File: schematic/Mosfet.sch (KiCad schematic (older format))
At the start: 35 parts, among them J10 Conn_01x03, J8 Screw_Terminal_01x02, J9 Conn_01x03, Q1 PSMN1R7-30YL, Q2 PSMN1R7-30YL, Q3 NCV8402, Q4 NCV8402

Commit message: Fixed C93 footprint
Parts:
- C93: footprint Resistors_SMD:R_0603 -> Capacitors_SMD:C_0603
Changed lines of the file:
@@
 F 0 "C93" H 9225 3150 50  0000 L CNN
 F 1 "100nF" H 9225 2950 50  0000 L CNN
-F 2 "Resistors_SMD:R_0603" H 9238 2900 50  0001 C CNN
+F 2 "Capacitors_SMD:C_0603" H 9238 2900 50  0001 C CNN
 F 3 "" H 9200 3050 50  0001 C CNN
 	1    9200 3050

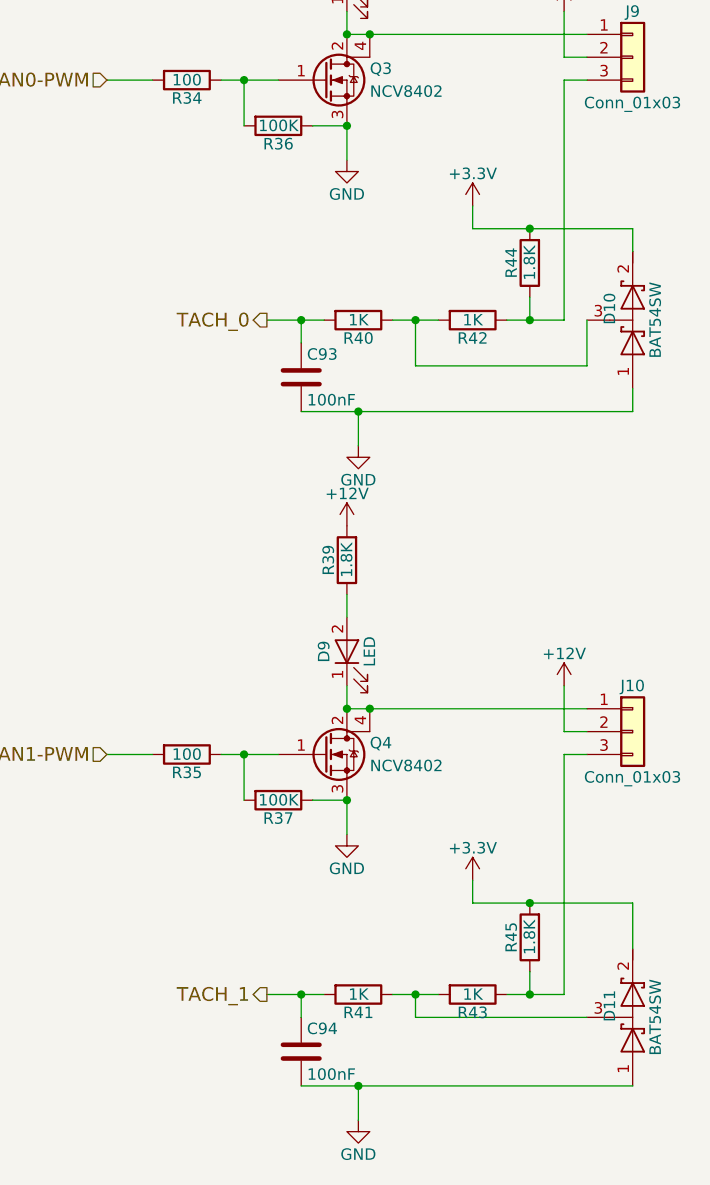
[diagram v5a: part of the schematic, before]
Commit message: Removed some components
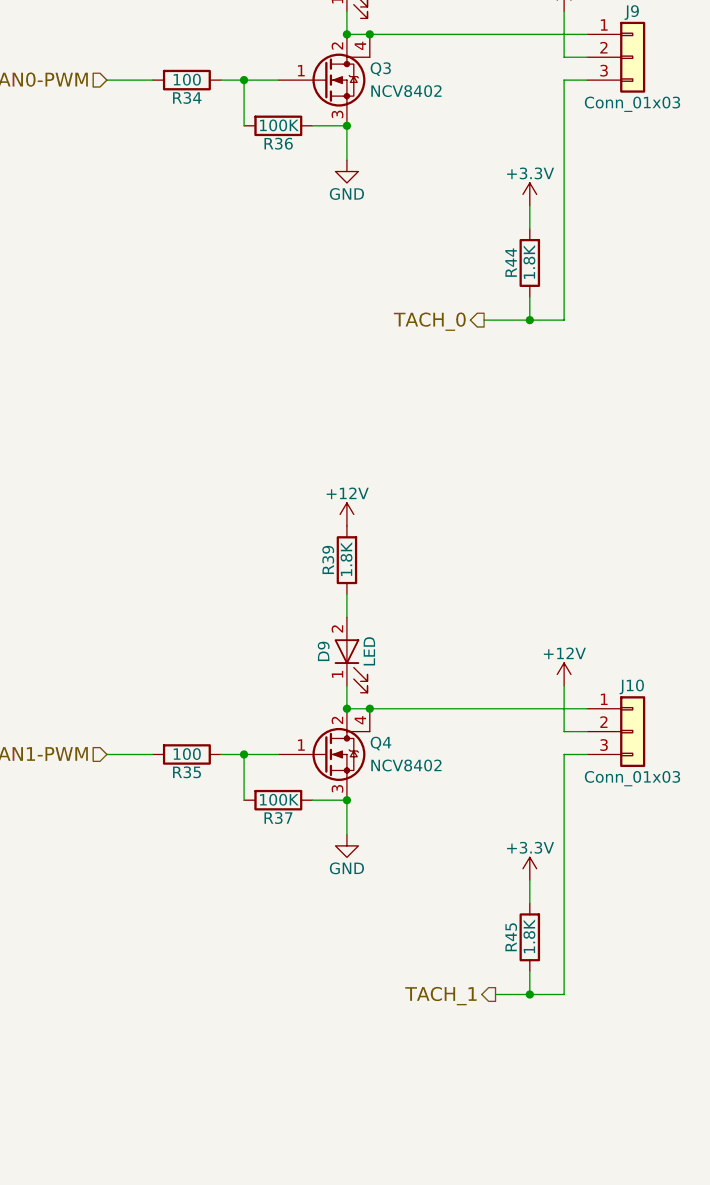
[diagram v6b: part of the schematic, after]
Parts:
- removed C93, C94: 100nF, Capacitors_SMD:C_0603, symbol C
- removed D10, D11: BAT54SW, TO_SOT_Packages_SMD:SOT-323_SC-70, symbol D_Schottky_x2_Serial_AKC
- removed R40, R41, R42, R43: 1K, Resistors_SMD:R_0603, symbol R
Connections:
- net TACH_0: now also J9.3 (Pin_3), R44.1
- net TACH_1: now also J10.3 (Pin_3), R45.1
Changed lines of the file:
@@
 	9400 1950 9400 2100
 $Comp
-L GND #PWR119
+L GND #PWR121
 U 1 1 59EA915F
 P 9400 2100
-F 0 "#PWR119" H 9400 1850 50  0001 C CNN
+F 0 "#PWR121" H 9400 1850 50  0001 C CNN
 F 1 "GND" H 9400 1950 50  0000 C CNN
 F 2 "" H 9400 2100 50  0001 C CNN
@@
 $EndComp
 $Comp
-L +12V #PWR126
+L +12V #PWR120
 U 1 1 59EBB7E0
 P 10350 1450
-F 0 "#PWR126" H 10350 1300 50  0001 C CNN
+F 0 "#PWR120" H 10350 1300 50  0001 C CNN
 F 1 "+12V" H 10350 1590 50  0000 C CNN
 F 2 "" H 10350 1450 50  0001 C CNN
@@
 Wire Wire Line
 	10350 1650 10350 1450
-$Comp
-L R R40
-U 1 1 59EBB878
-P 9450 2800
-F 0 "R40" V 9530 2800 50  0000 C CNN
-F 1 "1K" V 9450 2800 50  0000 C CNN
-F 2 "Resistors_SMD:R_0603" V 9380 2800 50  0001 C CNN
-F 3 "" H 9450 2800 50  0001 C CNN
-	1    9450 2800
-	0    1    1    0
-$EndComp
-$Comp
-L R R42
-U 1 1 59EBB8DD
-P 9950 2800
-F 0 "R42" V 10030 2800 50  0000 C CNN
-F 1 "1K" V 9950 2800 50  0000 C CNN
-F 2 "Resistors_SMD:R_0603" V 9880 2800 50  0001 C CNN
-F 3 "" H 9950 2800 50  0001 C CNN
-	1    9950 2800
-	0    1    1    0
-$EndComp
 $Comp
 L R R44
@@
 	-1   0    0    1
 $EndComp
-$Comp
-L C C93
-U 1 1 59EBB948
-P 9200 3050
-F 0 "C93" H 9225 3150 50  0000 L CNN
-F 1 "100nF" H 9225 2950 50  0000 L CNN
-F 2 "Capacitors_SMD:C_0603" H 9238 2900 50  0001 C CNN
-F 3 "" H 9200 3050 50  0001 C CNN
-	1    9200 3050
-	1    0    0    -1
-$EndComp
 Wire Wire Line
 	10450 1750 10350 1750
@@
 	10350 1750 10350 2800
 Wire Wire Line
-	10350 2800 10100 2800
+	10350 2800 10000 2800
 Wire Wire Line
 	10200 2800 10200 2700
 Connection ~ 10200 2800
-Wire Wire Line
-	9600 2800 9800 2800
-Connection ~ 9700 2800
-Wire Wire Line
-	9200 3200 10650 3200
-Wire Wire Line
-	9200 2900 9200 2800
-Wire Wire Line
-	9050 2800 9300 2800
-$Comp
-L GND #PWR122
-U 1 1 59EBBD19
-P 9450 3350
-F 0 "#PWR122" H 9450 3100 50  0001 C CNN
-F 1 "GND" H 9450 3200 50  0000 C CNN
-F 2 "" H 9450 3350 50  0001 C CNN
-F 3 "" H 9450 3350 50  0001 C CNN
-	1    9450 3350
-	1    0    0    -1
-$EndComp
-Wire Wire Line
-	9450 3350 9450 3200
-Connection ~ 9450 3200
-Connection ~ 9200 2800
-Text HLabel 9050 2800 0    60   Output ~ 0
+Text HLabel 10000 2800 0    60   Output ~ 0
 TACH_0
 $Comp
-L +3.3V #PWR124
+L +3.3V #PWR122
 U 1 1 59EBBF65
-P 9950 2300
-F 0 "#PWR124" H 9950 2150 50  0001 C CNN
-F 1 "+3.3V" H 9950 2440 50  0000 C CNN
-F 2 "" H 9950 2300 50  0001 C CNN
-F 3 "" H 9950 2300 50  0001 C CNN
-	1    9950 2300
-	1    0    0    -1
-$EndComp
-Wire Wire Line
-	9950 2300 9950 2400
+P 10200 2300
+F 0 "#PWR122" H 10200 2150 50  0001 C CNN
+F 1 "+3.3V" H 10200 2440 50  0000 C CNN
+F 2 "" H 10200 2300 50  0001 C CNN
+F 3 "" H 10200 2300 50  0001 C CNN
+	1    10200 2300
+	1    0    0    -1
+$EndComp
+Wire Wire Line
+	10200 2300 10200 2400
 $Comp
 L Q_NMOS_GDSD Q4
@@
 	9400 4900 9400 5050
 $Comp
-L GND #PWR121
+L GND #PWR128
 U 1 1 59EBE910
 P 9400 5050
-F 0 "#PWR121" H 9400 4800 50  0001 C CNN
+F 0 "#PWR128" H 9400 4800 50  0001 C CNN
 F 1 "GND" H 9400 4900 50  0000 C CNN
 F 2 "" H 9400 5050 50  0001 C CNN
@@
 	8350 4700 8550 4700
 $Comp
-L +12V #PWR120
+L +12V #PWR125
 U 1 1 59EBE919
 P 9400 3700
-F 0 "#PWR120" H 9400 3550 50  0001 C CNN
+F 0 "#PWR125" H 9400 3550 50  0001 C CNN
 F 1 "+12V" H 9400 3840 50  0000 C CNN
 F 2 "" H 9400 3700 50  0001 C CNN
@@
 $EndComp
 $Comp
-L +12V #PWR127
+L +12V #PWR126
 U 1 1 59EBE91F
 P 10350 4400
-F 0 "#PWR127" H 10350 4250 50  0001 C CNN
+F 0 "#PWR126" H 10350 4250 50  0001 C CNN
 F 1 "+12V" H 10350 4540 50  0000 C CNN
 F 2 "" H 10350 4400 50  0001 C CNN
@@
 Wire Wire Line
 	10350 4600 10350 4400
-$Comp
-L R R41
-U 1 1 59EBE927
-P 9450 5750
-F 0 "R41" V 9530 5750 50  0000 C CNN
-F 1 "1K" V 9450 5750 50  0000 C CNN
-F 2 "Resistors_SMD:R_0603" V 9380 5750 50  0001 C CNN
-F 3 "" H 9450 5750 50  0001 C CNN
-	1    9450 5750
-	0    1    1    0
-$EndComp
-$Comp
-L R R43
-U 1 1 59EBE92D
-P 9950 5750
-F 0 "R43" V 10030 5750 50  0000 C CNN
-F 1 "1K" V 9950 5750 50  0000 C CNN
-F 2 "Resistors_SMD:R_0603" V 9880 5750 50  0001 C CNN
-F 3 "" H 9950 5750 50  0001 C CNN
-	1    9950 5750
-	0    1    1    0
-$EndComp
 $Comp
 L R R45
@@
 	-1   0    0    1
 $EndComp
-$Comp
-L C C94
-U 1 1 59EBE939
-P 9200 6000
-F 0 "C94" H 9225 6100 50  0000 L CNN
-F 1 "100nF" H 9225 5900 50  0000 L CNN
-F 2 "Capacitors_SMD:C_0603" H 9238 5850 50  0001 C CNN
-F 3 "" H 9200 6000 50  0001 C CNN
-	1    9200 6000
-	1    0    0    -1
-$EndComp
 Wire Wire Line
 	10450 4700 10350 4700
@@
 	10350 4700 10350 5750
 Wire Wire Line
-	10350 5750 10100 5750
+	10350 5750 10050 5750
 Wire Wire Line
 	10200 5750 10200 5650
 Connection ~ 10200 5750
 Wire Wire Line
-	9600 5750 9800 5750
-Connection ~ 9700 5750
-Wire Wire Line
-	9950 5350 10650 5350
-Wire Wire Line
-	9200 6150 10650 6150
-Wire Wire Line
-	9200 5850 9200 5750
-Wire Wire Line
-	9050 5750 9300 5750
-$Comp
-L GND #PWR123
-U 1 1 59EBE957
-P 9450 6300
-F 0 "#PWR123" H 9450 6050 50  0001 C CNN
-F 1 "GND" H 9450 6150 50  0000 C CNN
-F 2 "" H 9450 6300 50  0001 C CNN
-F 3 "" H 9450 6300 50  0001 C CNN
-	1    9450 6300
-	1    0    0    -1
-$EndComp
-Wire Wire Line
-	9450 6300 9450 6150
-Connection ~ 9450 6150
-Connection ~ 9200 5750
-Text HLabel 9050 5750 0    60   Output ~ 0
+	10200 5350 10200 5350
+Text HLabel 10050 5750 0    60   Output ~ 0
 TACH_1
 $Comp
-L +3.3V #PWR125
+L +3.3V #PWR129
 U 1 1 59EBE961
-P 9950 5250
-F 0 "#PWR125" H 9950 5100 50  0001 C CNN
-F 1 "+3.3V" H 9950 5390 50  0000 C CNN
-F 2 "" H 9950 5250 50  0001 C CNN
-F 3 "" H 9950 5250 50  0001 C CNN
-	1    9950 5250
-	1    0    0    -1
-$EndComp
-Wire Wire Line
-	9950 5250 9950 5350
+P 10200 5250
+F 0 "#PWR129" H 10200 5100 50  0001 C CNN
+F 1 "+3.3V" H 10200 5390 50  0000 C CNN
+F 2 "" H 10200 5250 50  0001 C CNN
+F 3 "" H 10200 5250 50  0001 C CNN
+	1    10200 5250
+	1    0    0    -1
+$EndComp
+Wire Wire Line
+	10200 5250 10200 5350
 Text HLabel 1700 2200 0    60   Input ~ 0
 BED
@@
 $EndComp
 $Comp
-L +24V #PWR114
+L +24V #PWR119
 U 1 1 59EC2711
 P 2350 1400
-F 0 "#PWR114" H 2350 1250 50  0001 C CNN
+F 0 "#PWR119" H 2350 1250 50  0001 C CNN
 F 1 "+24V" H 2350 1540 50  0000 C CNN
 F 2 "" H 2350 1400 50  0001 C CNN
@@
 	2350 2950 2350 2900
 $Comp
-L GND #PWR115
+L GND #PWR123
 U 1 1 59EC2B99
 P 2350 2950
-F 0 "#PWR115" H 2350 2700 50  0001 C CNN
+F 0 "#PWR123" H 2350 2700 50  0001 C CNN
 F 1 "GND" H 2350 2800 50  0000 C CNN
 F 2 "" H 2350 2950 50  0001 C CNN
@@
 	2350 4950 2350 4900
 $Comp
-L GND #PWR117
+L GND #PWR127
 U 1 1 59EC3896
 P 2350 4950
-F 0 "#PWR117" H 2350 4700 50  0001 C CNN
+F 0 "#PWR127" H 2350 4700 50  0001 C CNN
 F 1 "GND" H 2350 4800 50  0000 C CNN
 F 2 "" H 2350 4950 50  0001 C CNN
@@
 Connection ~ 1950 4650
 $Comp
-L VBUS #PWR116
+L VBUS #PWR124
 U 1 1 59EC3DE5
 P 2350 3400
-F 0 "#PWR116" H 2350 3250 50  0001 C CNN
+F 0 "#PWR124" H 2350 3250 50  0001 C CNN
 F 1 "VBUS" H 2350 3550 50  0000 C CNN
 F 2 "" H 2350 3400 50  0001 C CNN
@@
 	1700 3600 1700 4200
 $Comp
-L D_Schottky_x2_Serial_AKC D10
-U 1 1 59F5BB09
-P 10650 2800
-F 0 "D10" H 10700 2700 50  0000 C CNN
-F 1 "BAT54SW" H 10650 2900 50  0000 C CNN
-F 2 "TO_SOT_Packages_SMD:SOT-323_SC-70" H 10650 2800 50  0001 C CNN
-F 3 "" H 10650 2800 50  0001 C CNN
-	1    10650 2800
-	0    1    -1   0
-$EndComp
-Wire Wire Line
-	10650 3200 10650 3100
-Wire Wire Line
-	10650 2400 10650 2500
-Connection ~ 10200 2400
-Wire Wire Line
-	9700 2800 9700 3000
-Wire Wire Line
-	9700 3000 10450 3000
-Wire Wire Line
-	10450 3000 10450 2800
-Wire Wire Line
-	9950 2400 10650 2400
-$Comp
-L D_Schottky_x2_Serial_AKC D11
-U 1 1 59F5C8FB
-P 10650 5850
-F 0 "D11" H 10700 5750 50  0000 C CNN
-F 1 "BAT54SW" H 10650 5950 50  0000 C CNN
-F 2 "TO_SOT_Packages_SMD:SOT-323_SC-70" H 10650 5850 50  0001 C CNN
-F 3 "" H 10650 5850 50  0001 C CNN
-	1    10650 5850
-	0    1    -1   0
-$EndComp
-Wire Wire Line
-	10450 5850 9700 5850
-Wire Wire Line
-	9700 5850 9700 5750
-Wire Wire Line
-	10650 5350 10650 5550
-Connection ~ 10200 5350
-$Comp
 L Screw_Terminal_01x02 J8

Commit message: Updated to kicad v5
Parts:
- D4, D5: symbol D_Schottky -> schematic-rescue:D_Schottky
- D6, D7, D8, D9: symbol LED -> schematic-rescue:LED
- J10, J9: symbol Conn_01x03 -> schematic-rescue:Conn_01x03
- J8: symbol Screw_Terminal_01x02 -> schematic-rescue:Screw_Terminal_01x02
- Q1, Q2: symbol PSMN1 -> psmn1:PSMN1
- Q3, Q4: symbol Q_NMOS_GDSD -> schematic-rescue:Q_NMOS_GDSD
- R28, R29, R30, R31, R32, R33, R34, R35, R36, R37, R38, R39, R44, R45: symbol R -> schematic-rescue:R
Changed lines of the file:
@@
-EESchema Schematic File Version 2
-LIBS:bd9e302efj
-LIBS:psmn1
-LIBS:tmc2130
-LIBS:74xgxx
-LIBS:74xx
-LIBS:ac-dc
-LIBS:actel
-LIBS:adc-dac
-LIBS:allegro
-LIBS:Altera
-LIBS:analog_devices
-LIBS:analog_switches
-LIBS:atmel
-LIBS:audio
-LIBS:battery_management
-LIBS:bbd
-LIBS:bosch
-LIBS:brooktre
-LIBS:cmos4000
-LIBS:cmos_ieee
-LIBS:conn
-LIBS:contrib
-LIBS:cypress
-LIBS:dc-dc
-LIBS:device
-LIBS:digital-audio
-LIBS:diode
-LIBS:display
-LIBS:dsp
-LIBS:elec-unifil
-LIBS:ESD_Protection
-LIBS:ftdi
-LIBS:gennum
-LIBS:graphic_symbols
-LIBS:hc11
-LIBS:infineon
-LIBS:intel
-LIBS:interface
-LIBS:intersil
-LIBS:ir
-LIBS:Lattice
-LIBS:leds
-LIBS:LEM
-LIBS:linear
-LIBS:logic_programmable
-LIBS:maxim
-LIBS:mechanical
-LIBS:memory
-LIBS:microchip
-LIBS:microchip_dspic33dsc
-LIBS:microchip_pic10mcu
-LIBS:microchip_pic12mcu
-LIBS:microchip_pic16mcu
-LIBS:microchip_pic18mcu
-LIBS:microchip_pic24mcu
-LIBS:microchip_pic32mcu
-LIBS:microcontrollers
-LIBS:modules
-LIBS:motor_drivers
-LIBS:motorola
-LIBS:motors
-LIBS:msp430
-LIBS:nordicsemi
-LIBS:nxp
-LIBS:nxp_armmcu
-LIBS:onsemi
-LIBS:opto
-LIBS:Oscillators
-LIBS:philips
-LIBS:power
-LIBS:powerint
-LIBS:Power_Management
-LIBS:pspice
-LIBS:references
-LIBS:regul
-LIBS:relays
-LIBS:rfcom
-LIBS:RFSolutions
-LIBS:sensors
-LIBS:silabs
-LIBS:siliconi
-LIBS:stm8
-LIBS:stm32
-LIBS:supertex
-LIBS:switches
-LIBS:texas
-LIBS:transf
-LIBS:transistors
-LIBS:triac_thyristor
-LIBS:ttl_ieee
-LIBS:valves
-LIBS:video
-LIBS:wiznet
-LIBS:Worldsemi
-LIBS:Xicor
-LIBS:xilinx
-LIBS:zetex
-LIBS:Zilog
+EESchema Schematic File Version 4
 LIBS:schematic-cache
-EELAYER 25 0
+EELAYER 26 0
 EELAYER END
 $Descr A4 11693 8268
@@
 BED-PWM
 $Comp
-L Q_NMOS_GDSD Q3
+L schematic-rescue:Q_NMOS_GDSD Q3
 U 1 1 59EA6010
 P 9300 1750
@@
 $EndComp
 $Comp
-L R R34
+L schematic-rescue:R R34
 U 1 1 59EA6171
 P 8700 1750
@@
 $EndComp
 $Comp
-L R R36
+L schematic-rescue:R R36
 U 1 1 59EA61EE
 P 9100 1950
@@
 $EndComp
 $Comp
-L R R38
+L schematic-rescue:R R38
 U 1 1 59EA6210
 P 9400 900
@@
 $EndComp
 $Comp
-L LED D8
+L schematic-rescue:LED D8
 U 1 1 59EA629A
 P 9400 1300
@@
 $EndComp
 $Comp
-L Conn_01x03 J9
+L schematic-rescue:Conn_01x03 J9
 U 1 1 59EA6367
 P 10650 1650
@@
 	9400 1950 9400 2100
 $Comp
-L GND #PWR0119
+L power:GND #PWR0119
 U 1 1 59EA915F
 P 9400 2100
@@
 	8350 1750 8550 1750
 $Comp
-L +12V #PWR0120
+L power:+12V #PWR0120
 U 1 1 59EBB7C2
 P 9400 750
@@
 $EndComp
 $Comp
-L +12V #PWR0121
+L power:+12V #PWR0121
 U 1 1 59EBB7E0
 P 10350 1450
@@
 	10350 1650 10350 1450
 $Comp
-L R R44
+L schematic-rescue:R R44
 U 1 1 59EBB904
 P 10200 2550
@@
 TACH_0
 $Comp
-L +3.3V #PWR0122
+L power:+3.3V #PWR0122
 U 1 1 59EBBF65
 P 10200 2300
@@
 	10200 2300 10200 2400
 $Comp
-L Q_NMOS_GDSD Q4
+L schematic-rescue:Q_NMOS_GDSD Q4
 U 1 1 59EBE8E2
 P 9300 4700
@@
 $EndComp
 $Comp
-L R R35
+L schematic-rescue:R R35
 U 1 1 59EBE8E8
 P 8700 4700
@@
 $EndComp
 $Comp
-L R R37
+L schematic-rescue:R R37
 U 1 1 59EBE8EE
 P 9100 4900
@@
 $EndComp
 $Comp
-L R R39
+L schematic-rescue:R R39
 U 1 1 59EBE8F4
 P 9400 3850
@@
 $EndComp
 $Comp
-L LED D9
+L schematic-rescue:LED D9
 U 1 1 59EBE8FA
 P 9400 4250
@@
 $EndComp
 $Comp
-L Conn_01x03 J10
+L schematic-rescue:Conn_01x03 J10
 U 1 1 59EBE900
 P 10650 4600
@@
 	9400 4900 9400 5050
 $Comp
-L GND #PWR0123
+L power:GND #PWR0123
 U 1 1 59EBE910
 P 9400 5050
@@
 	8350 4700 8550 4700
 $Comp
-L +12V #PWR0124
+L power:+12V #PWR0124
 U 1 1 59EBE919
 P 9400 3700
@@
 $EndComp
 $Comp
-L +12V #PWR0125
+L power:+12V #PWR0125
 U 1 1 59EBE91F
 P 10350 4400
@@
 	10350 4600 10350 4400
 $Comp
-L R R45
+L schematic-rescue:R R45
 U 1 1 59EBE933
 P 10200 5500
@@
 TACH_1
 $Comp
-L +3.3V #PWR0126
+L power:+3.3V #PWR0126
 U 1 1 59EBE961
 P 10200 5250
@@
 BED
 $Comp
-L PSMN1 Q1
+L psmn1:PSMN1 Q1
 U 1 1 59EC1D43
 P 2250 2650
@@
 $EndComp
 $Comp
-L LED D6
+L schematic-rescue:LED D6
 U 1 1 59EC25C7
 P 2350 2050
@@
 $EndComp
 $Comp
-L R R32
+L schematic-rescue:R R32
 U 1 1 59EC2646
 P 2350 1650
@@
 $EndComp
 $Comp
-L +24V #PWR0127
+L power:+24V #PWR0127
 U 1 1 59EC2711
 P 2350 1400
@@
 $EndComp
 $Comp
-L D_Schottky D4
+L schematic-rescue:D_Schottky D4
 U 1 1 59EC2791
 P 2100 1850
@@
 	2350 2950 2350 2900
 $Comp
-L GND #PWR0128
+L power:GND #PWR0128
 U 1 1 59EC2B99
 P 2350 2950
@@
 $EndComp
 $Comp
-L R R28
+L schematic-rescue:R R28
 U 1 1 59EC2F12
 P 1650 2650
@@
 $EndComp
 $Comp
-L R R30
+L schematic-rescue:R R30
 U 1 1 59EC2FA6
 P 2100 2900
@@
 EXT-PWM
 $Comp
-L PSMN1 Q2
+L psmn1:PSMN1 Q2
 U 1 1 59EC386E
 P 2250 4650
@@
 $EndComp
 $Comp
-L LED D7
+L schematic-rescue:LED D7
 U 1 1 59EC3874
 P 2350 4050
@@
 $EndComp
 $Comp
-L R R33
+L schematic-rescue:R R33
 U 1 1 59EC387A
 P 2350 3650
@@
 $EndComp
 $Comp
-L D_Schottky D5
+L schematic-rescue:D_Schottky D5
 U 1 1 59EC3886
 P 2100 3850
@@
 	2350 4950 2350 4900
 $Comp
-L GND #PWR0129
+L power:GND #PWR0129
 U 1 1 59EC3896
 P 2350 4950
@@
 $EndComp
 $Comp
-L R R29
+L schematic-rescue:R R29
 U 1 1 59EC389C
 P 1650 4650
@@
 $EndComp
 $Comp
-L R R31
+L schematic-rescue:R R31
 U 1 1 59EC38A2
 P 2100 4900
@@
 Connection ~ 1950 4650
 $Comp
-L VBUS #PWR0130
+L power:VBUS #PWR0130
 U 1 1 59EC3DE5
 P 2350 3400
@@
 	1700 3600 1700 4200
 $Comp
-L Screw_Terminal_01x02 J8
+L schematic-rescue:Screw_Terminal_01x02 J8
 U 1 1 5A001F35
 P 1500 3600
